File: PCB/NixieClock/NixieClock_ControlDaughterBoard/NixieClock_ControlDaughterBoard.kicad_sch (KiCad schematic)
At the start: 32 parts, among them J1 Conn_01x05, J2 Conn_01x05, J3 Conn_01x04_Pin, J4 Conn_01x04_Pin, Q1 IRLML6244, Q2 IRLML6244

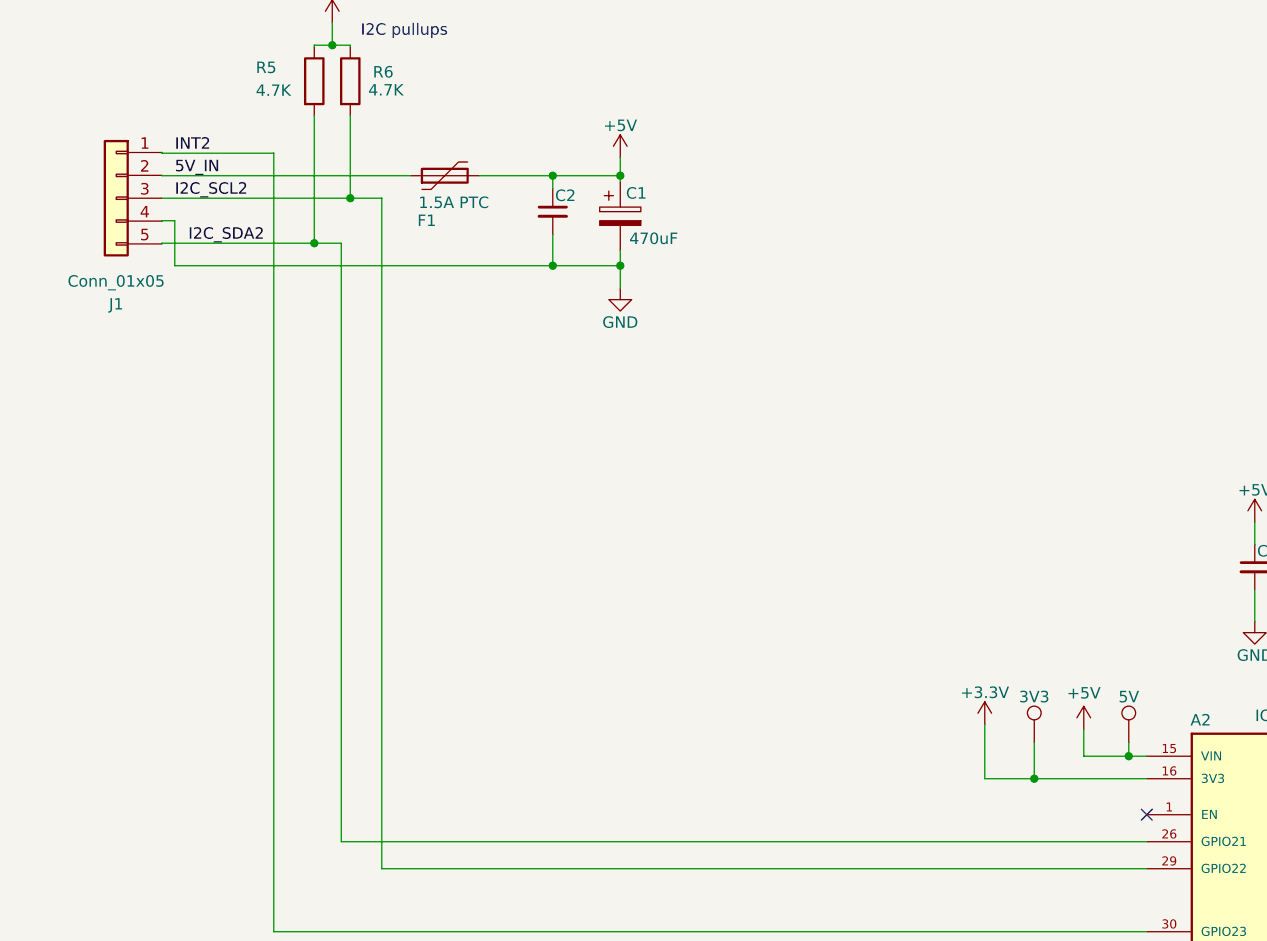
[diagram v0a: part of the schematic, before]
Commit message: Layout WIP
layout half completed.
+5V net class added to SCH so it has thicker traces on PCB
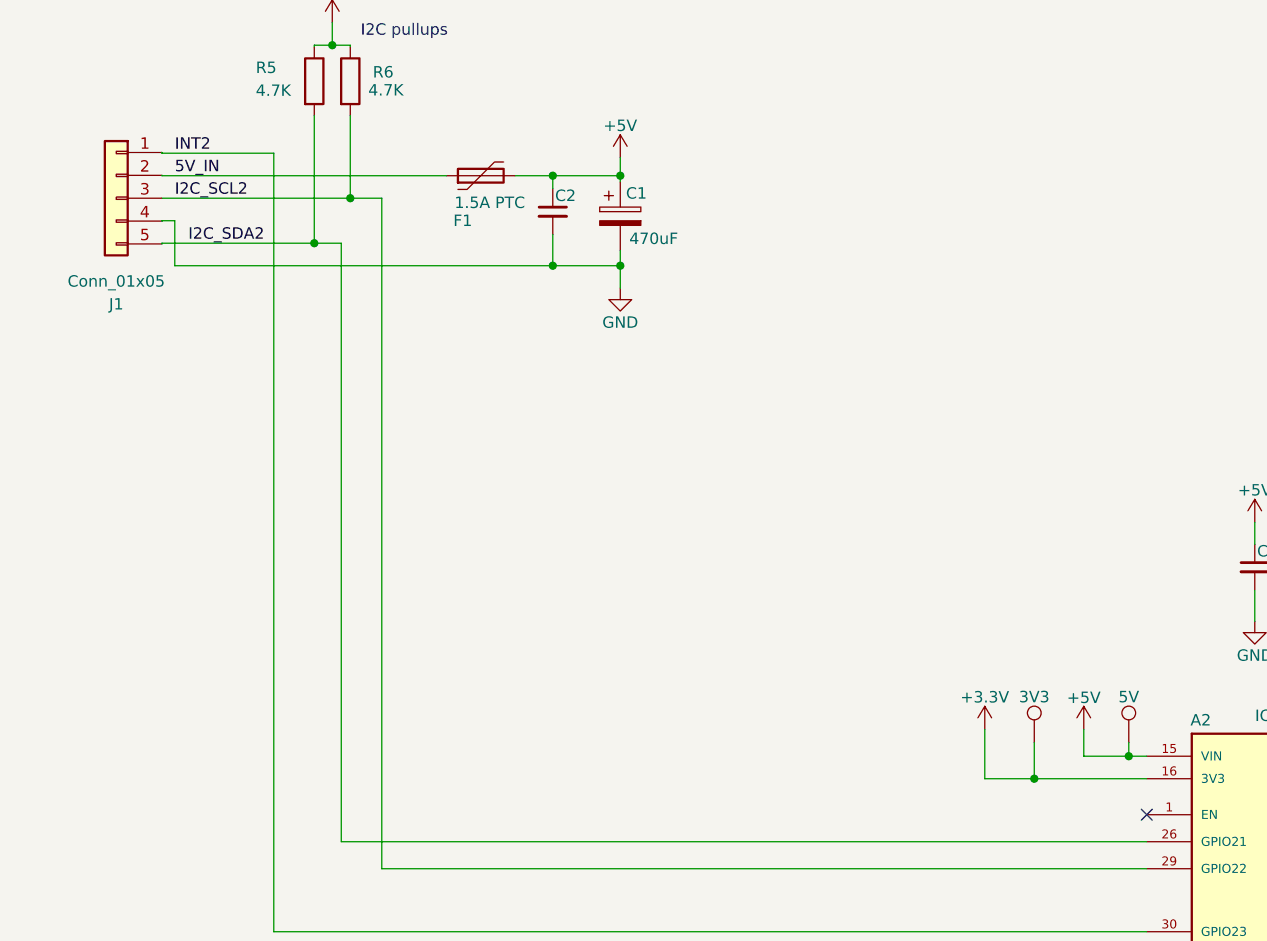
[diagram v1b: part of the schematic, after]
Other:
- moved on the sheet: F1
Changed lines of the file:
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@@
 	(wire
 		(pts
-			(xy 89.58 34.5) (xy 117.19 34.5)
+			(xy 89.58 34.5) (xy 121.19 34.5)
 		)
 		(stroke
@@
 	(wire
 		(pts
-			(xy 181 101.5) (xy 181 95.5)
+			(xy 181 101.5) (xy 181 96)
 		)
 		(stroke
@@
 	(wire
 		(pts
-			(xy 124.81 34.5) (xy 133 34.5)
+			(xy 128.81 34.5) (xy 133 34.5)
 		)
 		(stroke
@@
 		(length 1.5)
 		(shape round)
-		(at 298 28 0)
+		(at 112.5 34.5 0)
 		(fields_autoplaced yes)
 		(effects
@@
 			(justify left bottom)
 		)
-		(property "Netclass" "HighVoltage"
-			(at 298.6985 26.5 0)
+		(property "Netclass" "+5V"
+			(at 113.1985 33 0)
 			(effects
 				(font
@@
 		)
 		(property "Component Class" ""
-			(at 271 -30.5 0)
+			(at 85.5 -24 0)
 			(effects
 				(font
@@
 		(length 1.5)
 		(shape round)
-		(at 127 34.5 0)
+		(at 133 34.5 0)
 		(fields_autoplaced yes)
 		(effects
@@
 		)
 		(property "Netclass" "+5V"
-			(at 127.6985 33 0)
+			(at 133.6985 33 0)
 			(effects
 				(font
@@
 		)
 		(property "Component Class" ""
-			(at 100 -24 0)
+			(at 106 -24 0)
+			(effects
+				(font
+					(size 1.27 1.27)
+					(italic yes)
+				)
+			)
+		)
+	)
+	(netclass_flag ""
+		(length 1.5)
+		(shape round)
+		(at 298 28 0)
+		(fields_autoplaced yes)
+		(effects
+			(font
+				(size 1.27 1.27)
+			)
+			(justify left bottom)
+		)
+		(property "Netclass" "HighVoltage"
+			(at 298.6985 26.5 0)
+			(effects
+				(font
+					(size 1.27 1.27)
+				)
+				(justify left)
+			)
+		)
+		(property "Component Class" ""
+			(at 271 -30.5 0)
 			(effects
 				(font
@@
 		)
 		(property "Value" "+5V"
-			(at 192 92 0)
+			(at 192 92.5 0)
 			(effects
 				(font
@@
 	(symbol
 		(lib_id "Device:Polyfuse")
-		(at 121 34.5 90)
+		(at 125 34.5 90)
 		(unit 1)
 		(exclude_from_sim no)
@@
 		(dnp no)
 		(property "Reference" "F1"
-			(at 119 39.5 90)
+			(at 123 39.5 90)
 			(effects
 				(font
@@
 		)
 		(property "Value" "1.5A PTC"
-			(at 122 37.5 90)
+			(at 126 37.5 90)
 			(effects
 				(font
@@
 		)
 		(property "Footprint" "Resistor_SMD:R_1206_3216Metric_Pad1.30x1.75mm_HandSolder"
-			(at 126.08 33.23 0)
+			(at 130.08 33.23 0)
 			(effects
 				(font
@@
 		)
 		(property "Datasheet" "~"
-			(at 121 34.5 0)
+			(at 125 34.5 0)
 			(effects
 				(font
@@
 		)
 		(property "Description" "Resettable fuse, polymeric positive temperature coefficient"
-			(at 121 34.5 0)
+			(at 125 34.5 0)
 			(effects
 				(font
@@
 		)
 		(property "Company" ""
-			(at 121 34.5 0)
+			(at 125 34.5 0)
 			(effects
 				(font
@@
 		)
 		(property "Manufacturer" "Littelfuse"
-			(at 121 34.5 90)
+			(at 125 34.5 90)
 			(effects
 				(font
@@
 		)
 		(property "Manufacturer P/N" "NANOSMDC150F-2"
-			(at 121 34.5 90)
+			(at 125 34.5 90)
 			(effects
 				(font
@@
 		)
 		(property "Supplier" "Digikey"
-			(at 121 34.5 90)
+			(at 125 34.5 90)
 			(effects
 				(font
@@
 	(symbol
 		(lib_id "power:+3.3V")
-		(at 181 95.5 0)
+		(at 181 96 0)
 		(unit 1)
 		(exclude_from_sim no)
@@
 		(dnp no)
 		(property "Reference" "#PWR03"
-			(at 181 99.31 0)
+			(at 181 99.81 0)
 			(effects
 				(font
@@
 		)
 		(property "Value" "+3.3V"
-			(at 181 91.944 0)
+			(at 181 92.444 0)
 			(effects
 				(font
@@
 		)
 		(property "Footprint" ""
-			(at 181 95.5 0)
+			(at 181 96 0)
 			(effects
 				(font
@@
 		)
 		(property "Datasheet" ""
-			(at 181 95.5 0)
+			(at 181 96 0)
 			(effects
 				(font
@@
 		)
 		(property "Description" ""
-			(at 181 95.5 0)
+			(at 181 96 0)
 			(effects
 				(font
@@
 		)
 		(property "Company" ""
-			(at 181 95.5 0)
+			(at 181 96 0)
 			(effects
 				(font

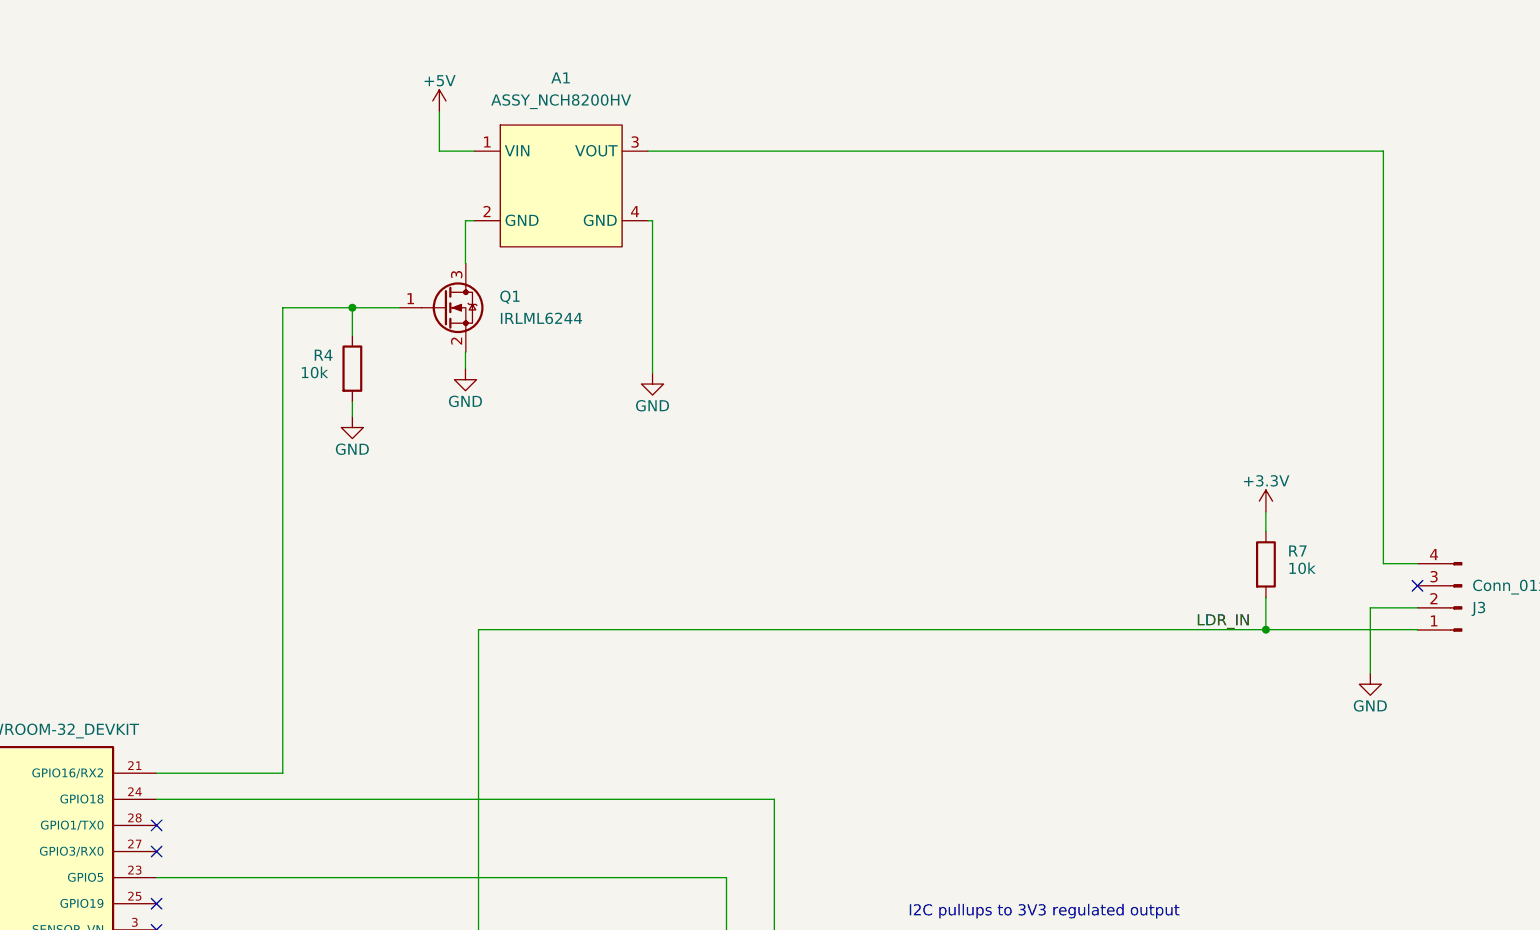
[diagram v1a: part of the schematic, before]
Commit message: Add current limit resistor to N-MOS base
needed to limit current into N-MOS during switching on. improves EMI and protects gate/esp driver from excessive current.
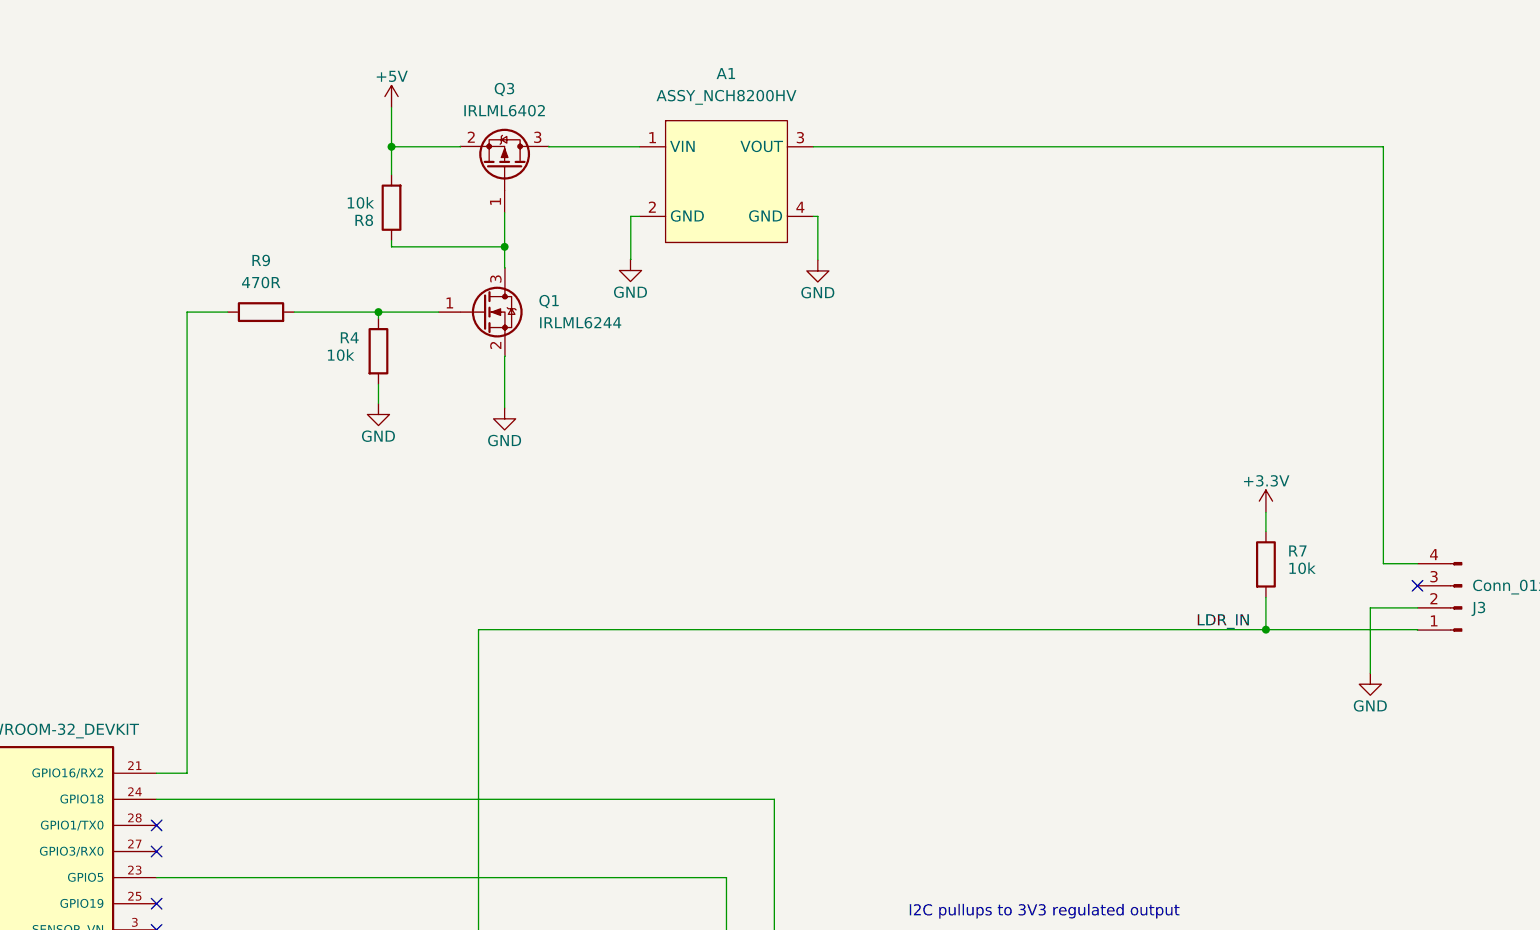
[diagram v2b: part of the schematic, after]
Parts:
- added Q3: IRLML6402, Package_TO_SOT_SMD:SOT-23, symbol Transistor_FET:IRLML6402
- added R8: 10k, Resistor_SMD:R_0805_2012Metric_Pad1.20x1.40mm_HandSolder, symbol Device:R
- added R9: 470R, Resistor_SMD:R_0805_2012Metric_Pad1.20x1.40mm_HandSolder, symbol Device:R
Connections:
- net +5V: now also Q3.2 (S), R8.2; no longer A1.1 (VIN)
- net GND: now also A1.2 (GND)
- net at Q1.3 (D): now also Q3.1 (G), R8.1; no longer A1.2 (GND)
- net at Q1.1 (G), R4.1: now also R9.2; no longer A2.21 (GPIO16/RX2)
- new net: A2.21 (GPIO16/RX2), R9.1
- new net: A1.1 (VIN), Q3.3 (D)
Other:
- moved on the sheet: A1, Q1, R4

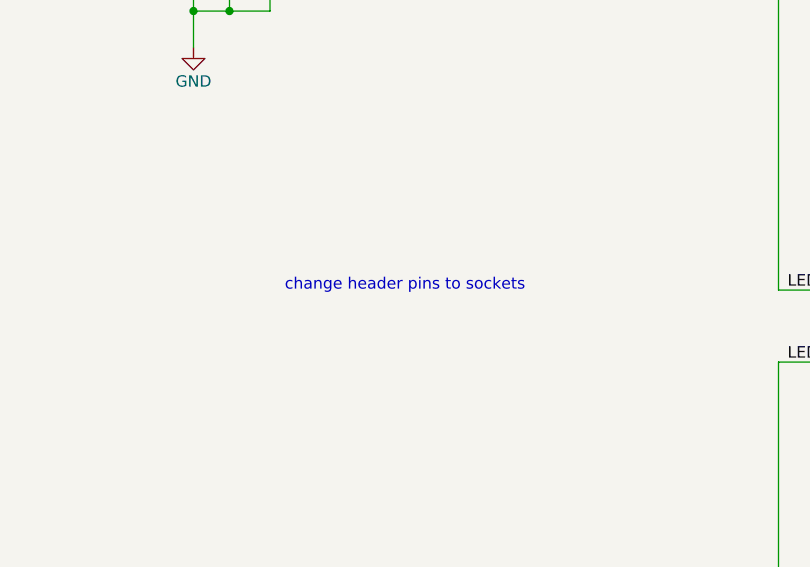
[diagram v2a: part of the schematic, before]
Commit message: remove text note to self
text note no longer needed
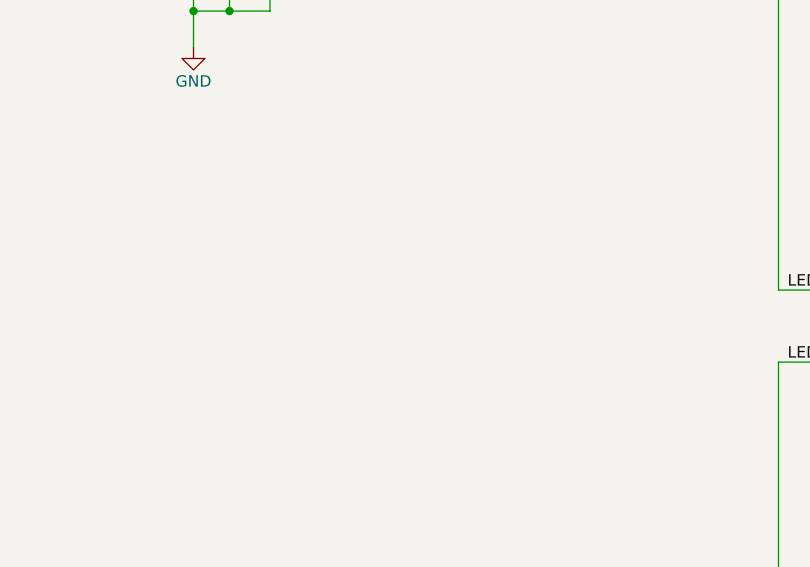
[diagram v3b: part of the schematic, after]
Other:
- note removed: "change header pins to sockets"
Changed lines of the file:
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@@
-		)
-	)
-	(text "change header pins to sockets"
-		(exclude_from_sim no)
-		(at 219 186.5 0)
-		(effects
-			(font
-				(size 1.27 1.27)
-			)
 		)
 	)
